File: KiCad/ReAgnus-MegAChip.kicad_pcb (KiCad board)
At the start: 2 copper layers, 78 x 49 mm, 52 parts, among them J1 Conn_02x05_Odd_Even, J2 Conn_02x02_Odd_Even, J3 Conn_01x03, U1 PLCC-84-Plug, U10 AS4C4M16SA, U11 74LVC245A, U12 74LVC1GX04, U2 LM1117-3.3, U3 SN74CBTD16210, U4 SN74CBTD16210, U5 SN74CBTD16210, U6 SN74CBTD16210, U7 GW1N-UV9LQ144, U8 74LVC1G07, U9 Agnus_TH_plug_pins, X1 SG-8002CA, Y1 CL=16pF

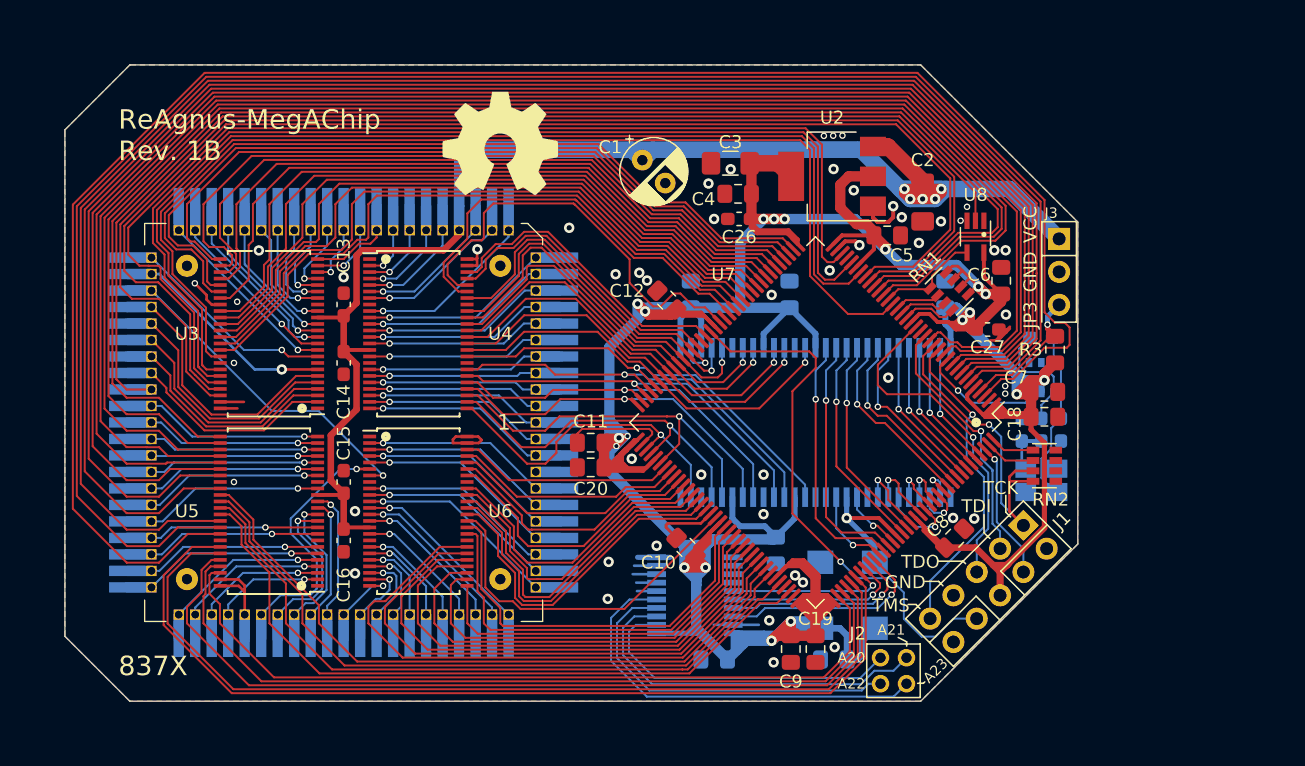
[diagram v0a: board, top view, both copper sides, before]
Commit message: Changed level shifters from SN74CBTD16210DGGR (TSSOP-48) to SN74CBT16210CDGVR (TVSOP-48) and added a 4.3V LDO regulator TPS73643DBV and re-routed.
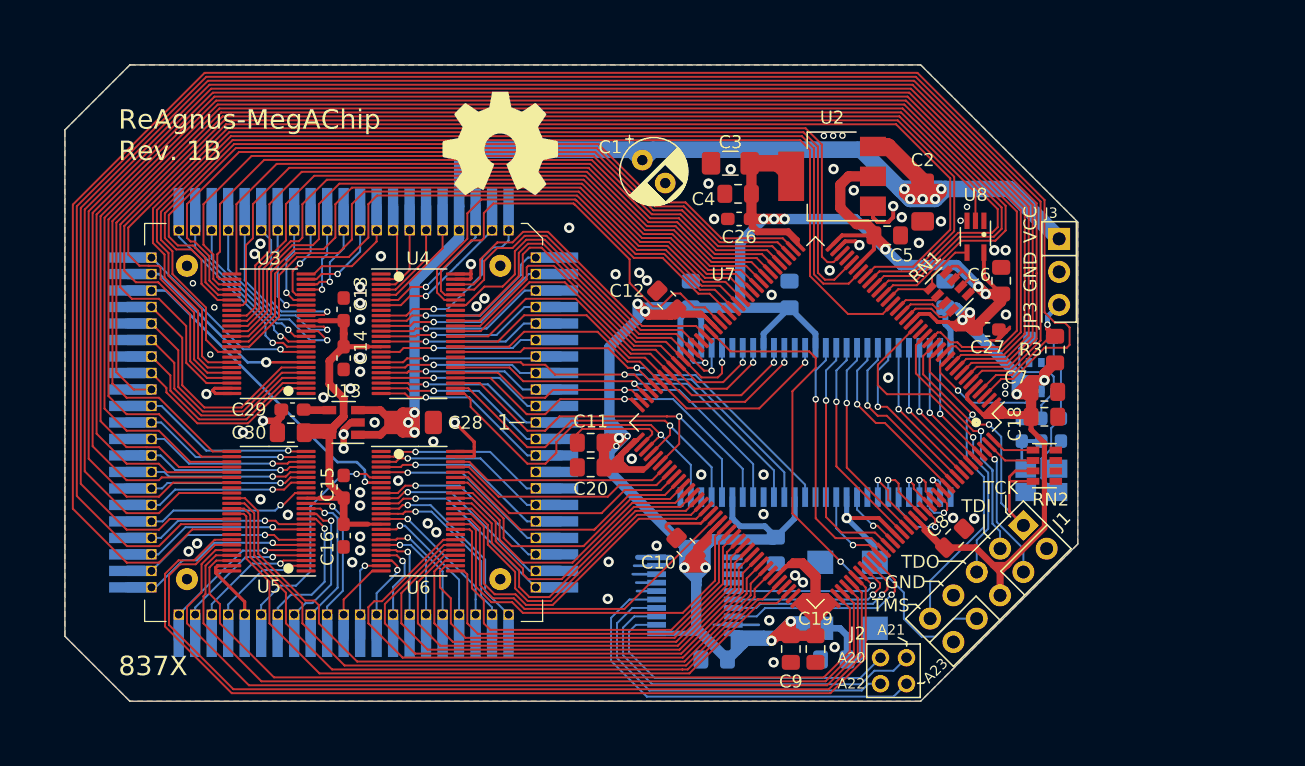
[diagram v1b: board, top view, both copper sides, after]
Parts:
- added C28: 10uF, Capacitor_SMD:C_1206_3216Metric_Pad1.33x1.80mm_HandSolder, F.Cu at (144.1, 114.8)
- added C29: 0.1uF, Capacitor_SMD:C_0603_1608Metric_Pad1.08x0.95mm_HandSolder, F.Cu at (134.8, 113.8)
- added C30: 10uF, Capacitor_SMD:C_0805_2012Metric_Pad1.18x1.45mm_HandSolder, F.Cu at (134.7, 115.6)
- added U13: TPS73643DBV, Package_TO_SOT_SMD:SOT-23-5, F.Cu at (138.8, 114.8)
- U3, U4, U5, U6: value SN74CBTD16210 -> SN74CBT16210; footprint Package_SO:TSSOP-48_6.1x12.5mm_P0.5mm -> Package_SO:TSSOP-48_4.4x9.7mm_P0.4mm
- moved C14 0.38 mm to (138.8, 109.9)
- moved C13 0.38 mm to (138.8, 106.1)
- moved C16 0.37 mm to (138.8, 123.5)
- moved C15 0.37 mm to (138.8, 119.8)
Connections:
- C13 pad 2: VCC -> 4V3
- C14 pad 2: VCC -> 4V3
- C15 pad 2: VCC -> 4V3
- C16 pad 2: VCC -> 4V3
- U3 pad 15: VCC -> 4V3
- U4 pad 15: VCC -> 4V3
- U5 pad 15: VCC -> 4V3
- U6 pad 15: VCC -> 4V3
- U7 pad 40: BLIT_3V3 -> REGEN_3V3
- U7 pad 41: WE_3V3 -> RW_3V3
- U7 pad 42: RW_3V3 -> WE_3V3
- U7 pad 43: REGEN_3V3 -> BLIT_3V3
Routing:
- net 4V3: track 0.00 -> 37.0 mm
- net REGEN_3V3: track 52.7 -> 59.8 mm
- net VCC: track 152.8 -> 146.3 mm, vias 5 -> 8
- net GND: track 60.7 -> 65.7 mm, vias 50 -> 77
- net BLIT_3V3: track 56.9 -> 52.2 mm
- net RGA6: track 12.0 -> 15.4 mm
- net RGA5: track 13.3 -> 16.7 mm
- net RGA7: track 10.8 -> 14.0 mm
- net RW_3V3: track 54.2 -> 57.0 mm
- net Net-(C29-Pad1): track 0.00 -> 1.99 mm
- net WE_3V3: track 56.4 -> 54.5 mm
- net A5_3V3: track 28.5 -> 30.4 mm
- net A19: track 20.9 -> 19.1 mm
- net BLISS_3V3: track 23.4 -> 25.1 mm
- net DRD15_3V3: track 26.0 -> 27.7 mm
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
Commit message: Changed to a four layer stackup, GND and a 3V3 as inner layers, added a MountingHole_2.2mm_M2 for proper grounding via a ring lug connector on a thick jumper wire
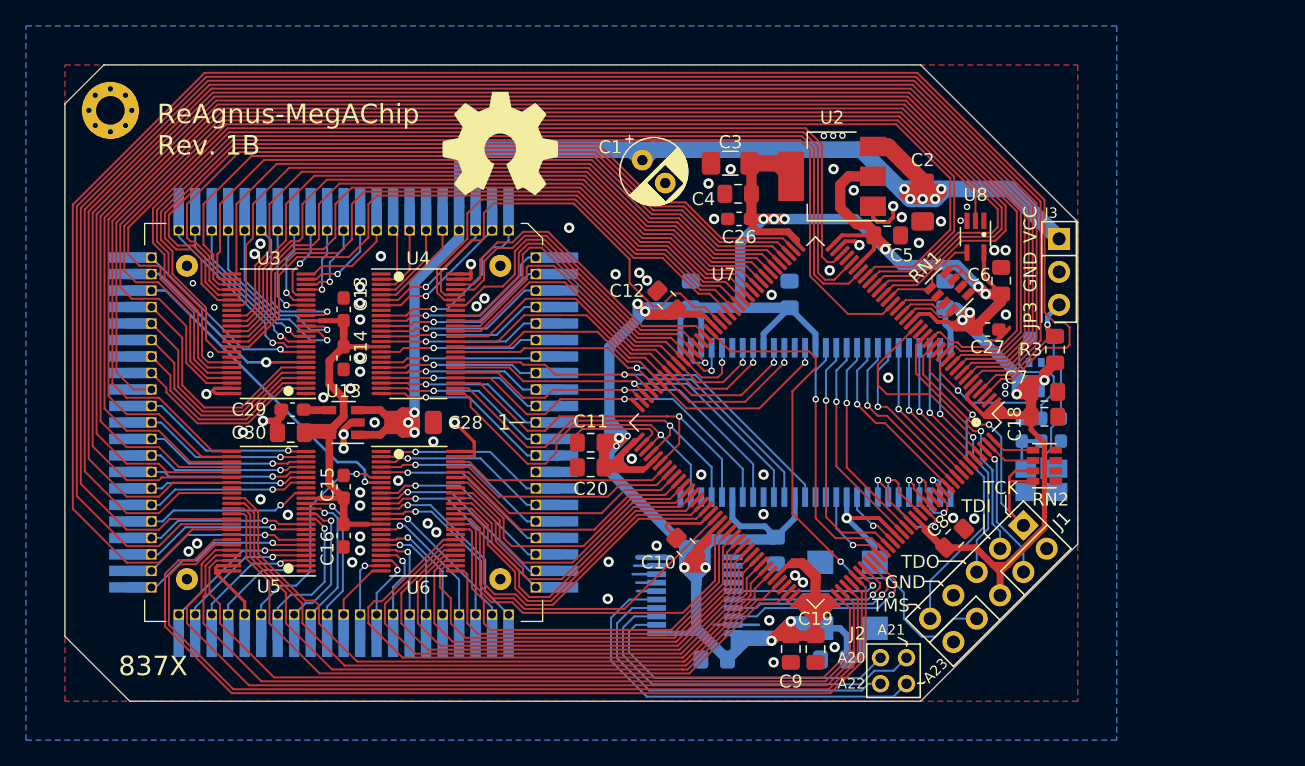
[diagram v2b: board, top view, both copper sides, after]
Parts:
- added J4: Conn_01x01, MountingHole:MountingHole_2.2mm_M2_Pad_Via, F.Cu at (120.8, 90.8)
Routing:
- added copper zone on 3V3.Cu, net 3V3
- added copper zone on GND.Cu, net GND
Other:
- outline, holes or cut-outs redrawn
- copper layers 2 -> 4
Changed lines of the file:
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@@
     (tracks 2592)
     (zones 0)
-    (modules 56)
+    (modules 57)
     (nets 225)
   )
@@
   (layers
     (0 F.Cu signal)
+    (1 GND.Cu power)
+    (2 3V3.Cu power)
     (31 B.Cu signal)
     (32 B.Adhes user)
@@
   )
   (setup
-    (last_trace_width 0.254)
+    (last_trace_width 0.1524)
     (user_trace_width 0.2032)
     (user_trace_width 0.2286)
@@
     (add_net nNTSC_8372_3V3)
   )
+  (module MountingHole:MountingHole_2.2mm_M2_Pad_Via (layer F.Cu)
+    (at 120.8 90.8)
+    (descr "Mounting Hole 2.2mm, M2")
+    (tags "mounting hole 2.2mm m2")
+    (zone_connect 2)
+    (attr virtual)
+    (fp_text reference J4 (at 0 -3.2) (layer F.SilkS) hide
+      (effects (font (size 1 1) (thickness 0.15)))
+    )
+    (fp_text value Conn_01x01 (at 0 3.2) (layer F.Fab) hide
+      (effects (font (size 1 1) (thickness 0.15)))
+    )
+    (fp_circle (center 0 0) (end 2.45 0) (layer F.CrtYd) (width 0.05))
+    (fp_circle (center 0 0) (end 2.2 0) (layer Cmts.User) (width 0.15))
+    (fp_text user %R (at 0.3 0) (layer F.Fab) hide
+      (effects (font (size 1 1) (thickness 0.15)))
+    )
+    (pad 1 thru_hole circle (at 1.166726 -1.166726) (size 0.7 0.7) (drill 0.4) (layers *.Cu *.Mask)
+      (net 2 GND) (zone_connect 2))
+    (pad 1 thru_hole circle (at 0 -1.65) (size 0.7 0.7) (drill 0.4) (layers *.Cu *.Mask)
+      (net 2 GND) (zone_connect 2))
+    (pad 1 thru_hole circle (at -1.166726 -1.166726) (size 0.7 0.7) (drill 0.4) (layers *.Cu *.Mask)
+      (net 2 GND) (zone_connect 2))
+    (pad 1 thru_hole circle (at -1.65 0) (size 0.7 0.7) (drill 0.4) (layers *.Cu *.Mask)
+      (net 2 GND) (zone_connect 2))
+    (pad 1 thru_hole circle (at -1.166726 1.166726) (size 0.7 0.7) (drill 0.4) (layers *.Cu *.Mask)
+      (net 2 GND) (zone_connect 2))
+    (pad 1 thru_hole circle (at 0 1.65) (size 0.7 0.7) (drill 0.4) (layers *.Cu *.Mask)
+      (net 2 GND) (zone_connect 2))
+    (pad 1 thru_hole circle (at 1.166726 1.166726) (size 0.7 0.7) (drill 0.4) (layers *.Cu *.Mask)
+      (net 2 GND) (zone_connect 2))
+    (pad 1 thru_hole circle (at 1.65 0) (size 0.7 0.7) (drill 0.4) (layers *.Cu *.Mask)
+      (net 2 GND) (zone_connect 2))
+    (pad 1 thru_hole circle (at 0 0) (size 4.4 4.4) (drill 2.2) (layers *.Cu *.Mask)
+      (net 2 GND) (zone_connect 2))
+  )
   (module Package_SO:TSSOP-48_4.4x9.7mm_P0.4mm (layer F.Cu)
     (at 144.5161 121.6662)
@@
     (fp_line (start 0 4.985) (end -2.2 4.985) (layer F.SilkS) (width 0.12))
     (fp_line (start 0 4.985) (end 2.2 4.985) (layer F.SilkS) (width 0.12))
+    (fp_circle (center -1.5 -4.4) (end -1.3 -4.4) (layer F.SilkS) (width 0.4))
     (fp_text user %R (at 0 0) (layer F.Fab) hide
       (effects (font (size 1 1) (thickness 0.15)))
     )
-    (fp_circle (center -1.5 -4.4) (end -1.3 -4.4) (layer F.SilkS) (width 0.4))
     (pad 48 smd roundrect (at 2.8625 -4.6) (size 1.475 0.25) (layers F.Cu F.Paste F.Mask) (roundrect_rratio 0.25)
       (net 2 GND) (zone_connect 0))
@@
     (fp_line (start 0 4.985) (end -2.2 4.985) (layer F.SilkS) (width 0.12))
     (fp_line (start 0 4.985) (end 2.2 4.985) (layer F.SilkS) (width 0.12))
+    (fp_circle (center -1.5 -4.4) (end -1.3 -4.4) (layer F.SilkS) (width 0.4))
     (fp_text user %R (at 0 0 180) (layer F.Fab) hide
       (effects (font (size 1 1) (thickness 0.15)))
     )
-    (fp_circle (center -1.5 -4.4) (end -1.3 -4.4) (layer F.SilkS) (width 0.4))
     (pad 48 smd roundrect (at 2.8625 -4.6 180) (size 1.475 0.25) (layers F.Cu F.Paste F.Mask) (roundrect_rratio 0.25)
       (net 2 GND) (zone_connect 0))
@@
     (fp_line (start 0 4.985) (end -2.2 4.985) (layer F.SilkS) (width 0.12))
     (fp_line (start 0 4.985) (end 2.2 4.985) (layer F.SilkS) (width 0.12))
+    (fp_circle (center -1.5 -4.4) (end -1.3 -4.4) (layer F.SilkS) (width 0.4))
     (fp_text user %R (at 0 0) (layer F.Fab) hide
       (effects (font (size 1 1) (thickness 0.15)))
     )
-    (fp_circle (center -1.5 -4.4) (end -1.3 -4.4) (layer F.SilkS) (width 0.4))
     (pad 48 smd roundrect (at 2.8625 -4.6 180) (size 1.475 0.25) (layers F.Cu F.Paste F.Mask) (roundrect_rratio 0.25)
       (net 2 GND) (zone_connect 0))
@@
     (fp_line (start 0.3 4.985) (end -2.2 4.985) (layer F.SilkS) (width 0.12))
     (fp_line (start 0.9 4.985) (end 2.2 4.985) (layer F.SilkS) (width 0.12))
+    (fp_circle (center -1.5 -4.4) (end -1.3 -4.4) (layer F.SilkS) (width 0.4))
     (fp_text user %R (at 0 0) (layer F.Fab) hide
       (effects (font (size 1 1) (thickness 0.15)))
     )
-    (fp_circle (center -1.5 -4.4) (end -1.3 -4.4) (layer F.SilkS) (width 0.4))
     (pad 48 smd roundrect (at 2.8625 -4.6) (size 1.475 0.25) (layers F.Cu F.Paste F.Mask) (roundrect_rratio 0.25)
       (net 2 GND) (zone_connect 0))
@@
   (gr_line (start 195.3 124.2) (end 183.2 136.3) (layer Edge.Cuts) (width 0.05))
   (gr_line (start 195.3 99.4) (end 183.2 87.3) (layer Edge.Cuts) (width 0.05))
-  (gr_line (start 122.3 87.3) (end 183.2 87.3) (layer Edge.Cuts) (width 0.05))
+  (gr_line (start 120.3 87.3) (end 183.2 87.3) (layer Edge.Cuts) (width 0.05))
   (gr_line (start 157.305 114.834) (end 158.405 114.834) (layer B.SilkS) (width 0.12))
   (gr_text 1 (at 159.21 114.834) (layer B.SilkS)
@@
     (effects (font (size 1 1) (thickness 0.15)))
   )
-  (gr_line (start 117.3 92.3) (end 122.3 87.3) (layer Edge.Cuts) (width 0.05))
-  (gr_line (start 117.3 131.3) (end 117.3 92.3) (layer Edge.Cuts) (width 0.05))
+  (gr_line (start 117.3 90.3) (end 120.3 87.3) (layer Edge.Cuts) (width 0.05))
+  (gr_line (start 117.3 131.3) (end 117.3 90.3) (layer Edge.Cuts) (width 0.05))
   (gr_line (start 183.2 136.3) (end 122.3 136.3) (layer Edge.Cuts) (width 0.05))
-  (gr_text "ReAgnus-MegAChip\nRev. 1B" (at 121.41988 92.72036) (layer F.SilkS)
+  (gr_text "ReAgnus-MegAChip\nRev. 1B" (at 124.4 92.3) (layer F.SilkS)
     (effects (font (size 1.5 1.5) (thickness 0.15)) (justify left))
   )
@@
     (polygon
       (pts
-        (xy 183.2 87.3) (xy 195.3 99.4) (xy 195.3 124.2) (xy 183.2 136.3) (xy 122.3 136.3)
-        (xy 117.3 131.3) (xy 117.3 92.3) (xy 122.3 87.3)
+        (xy 195.3 87.3) (xy 195.3 136.3) (xy 117.3 136.3) (xy 117.3 87.3)
       )
     )
@@
     (polygon
       (pts
-        (xy 183.2 87.3) (xy 195.3 99.4) (xy 195.3 124.2) (xy 183.2 136.3) (xy 122.3 136.3)
-        (xy 117.3 131.3) (xy 117.3 92.3) (xy 122.3 87.3)
+        (xy 198.3 84.3) (xy 198.3 139.3) (xy 114.3 139.3) (xy 114.3 84.3)
+      )
+    )
+  )
+  (zone (net 61) (net_name 3V3) (layer 3V3.Cu) (hatch edge 0.508)
+    (connect_pads (clearance 0.1524))
+    (min_thickness 0.254)
+    (fill yes (arc_segments 32) (thermal_gap 0.508) (thermal_bridge_width 0.508))
+    (polygon
+      (pts
+        (xy 197.3 138.3) (xy 115.3 138.3) (xy 115.3 85.3) (xy 197.3 85.3)
+      )
+    )
+  )
+  (zone (net 2) (net_name GND) (layer GND.Cu) (hatch edge 0.508)
+    (connect_pads (clearance 0.1524))
+    (min_thickness 0.254)
+    (fill yes (arc_segments 32) (thermal_gap 0.508) (thermal_bridge_width 0.508))
+    (polygon
+      (pts
+        (xy 196.3 137.3) (xy 116.3 137.3) (xy 116.3 86.3) (xy 196.3 86.3)
       )
     )

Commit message: Removed the SDRAM chip and the crystal oscillator
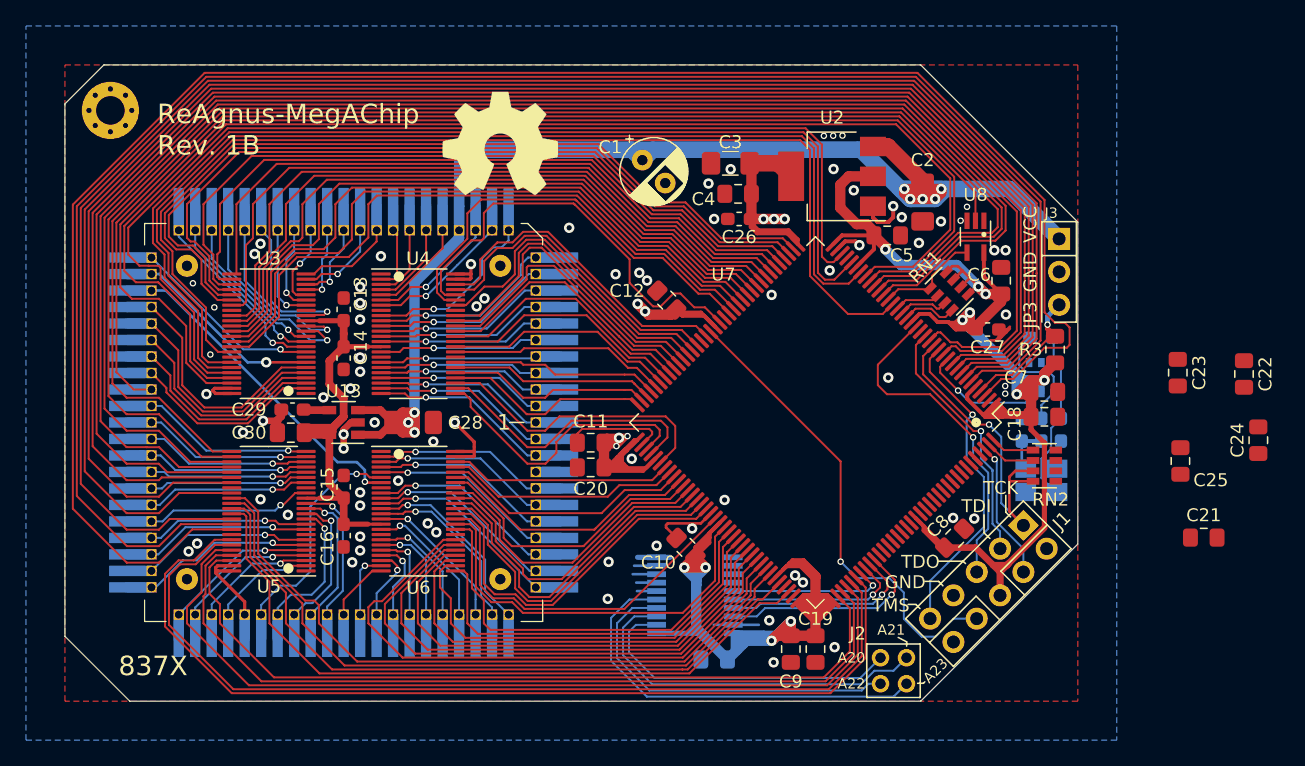
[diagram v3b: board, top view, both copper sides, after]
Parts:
- removed U10: AS4C4M16SA, Package_SO:TSOP-II-54_22.2x10.16mm_P0.8mm
- removed X1: SG-8002CA, Oscillator:Oscillator_SMD_SeikoEpson_SG8002CA-4Pin_7.0x5.0mm
- C21, C22, C23, C24, C25: moved to F.Cu
- moved C22 43.0 mm to (208.1, 111.1), turned to 270 degrees
- moved C25 31.9 mm to (203.2, 117.8), turned to 90 degrees
- moved C23 30.5 mm to (203.0, 111.0), turned to 270 degrees
- moved C21 30.0 mm to (205.0, 123.7)
- moved C24 26.6 mm to (209.2, 116.2), turned to 270 degrees
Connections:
- U7 pad 119: DQMH_SDRAM -> Net-(U7-Pad119)
- U7 pad 120: DQML_SDRAM -> Net-(U7-Pad120)
- U7 pad 121: WE_SDRAM -> Net-(U7-Pad121)
- U7 pad 122: CKE_SDRAM -> Net-(U7-Pad122)
- U7 pad 123: CLK_SDRAM -> Net-(U7-Pad123)
- U7 pad 124: CAS_SDRAM -> Net-(U7-Pad124)
- U7 pad 125: RAS_SDRAM -> Net-(U7-Pad125)
- U7 pad 126: A11_SDRAM -> Net-(U7-Pad126)
- U7 pad 128: A9_SDRAM -> Net-(U7-Pad128)
- U7 pad 129: A8_SDRAM -> Net-(U7-Pad129)
- U7 pad 130: A7_SDRAM -> Net-(U7-Pad130)
- U7 pad 131: A6_SDRAM -> Net-(U7-Pad131)
- U7 pad 132: A5_SDRAM -> Net-(U7-Pad132)
- U7 pad 133: A4_SDRAM -> Net-(U7-Pad133)
- U7 pad 134: CS_SDRAM -> Net-(U7-Pad134)
- U7 pad 135: BA0_SDRAM -> Net-(U7-Pad135)
- U7 pad 136: BA1_SDRAM -> Net-(U7-Pad136)
- U7 pad 137: A10_SDRAM -> Net-(U7-Pad137)
- U7 pad 138: A0_SDRAM -> Net-(U7-Pad138)
- U7 pad 139: A1_SDRAM -> Net-(U7-Pad139)
- U7 pad 140: A2_SDRAM -> Net-(U7-Pad140)
- U7 pad 141: A3_SDRAM -> Net-(U7-Pad141)
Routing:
- net 3V3: track 412.7 -> 288.6 mm
- net DQML_SDRAM: track 19.7 -> 0.00 mm, vias 1 -> 0
- net WE_SDRAM: track 19.1 -> 0.00 mm, vias 1 -> 0
- net DRD8_3V3: track 34.4 -> 16.7 mm, vias 1 -> 0
- net DRD9_3V3: track 33.3 -> 16.0 mm, vias 1 -> 0
- net CAS_SDRAM: track 16.6 -> 0.00 mm, vias 1 -> 0
- net RAS_SDRAM: track 16.1 -> 0.00 mm, vias 1 -> 0
- net DRD10_3V3: track 31.2 -> 15.6 mm, vias 1 -> 0
- net DRD11_3V3: track 30.5 -> 15.7 mm, vias 1 -> 0
- net DRD7_3V3: track 32.4 -> 17.8 mm, vias 1 -> 0
- net CS_SDRAM: track 14.3 -> 0.00 mm, vias 1 -> 0
- net BA0_SDRAM: track 13.7 -> 0.00 mm, vias 1 -> 0
- net DRD12_3V3: track 29.3 -> 15.8 mm, vias 1 -> 0
- net BA1_SDRAM: track 13.2 -> 0.00 mm, vias 1 -> 0
- net DRD6_3V3: track 31.3 -> 18.9 mm, vias 1 -> 0
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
